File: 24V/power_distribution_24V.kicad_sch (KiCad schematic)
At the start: 23 parts, among them J1 39-30-1040, J2 768250002, J3 39-30-1040, J4 172065-0002, J5 39-30-1040, J6 39-30-1040, J7 2002411213, J8 768250002, U1 RASPBERRY_PCB

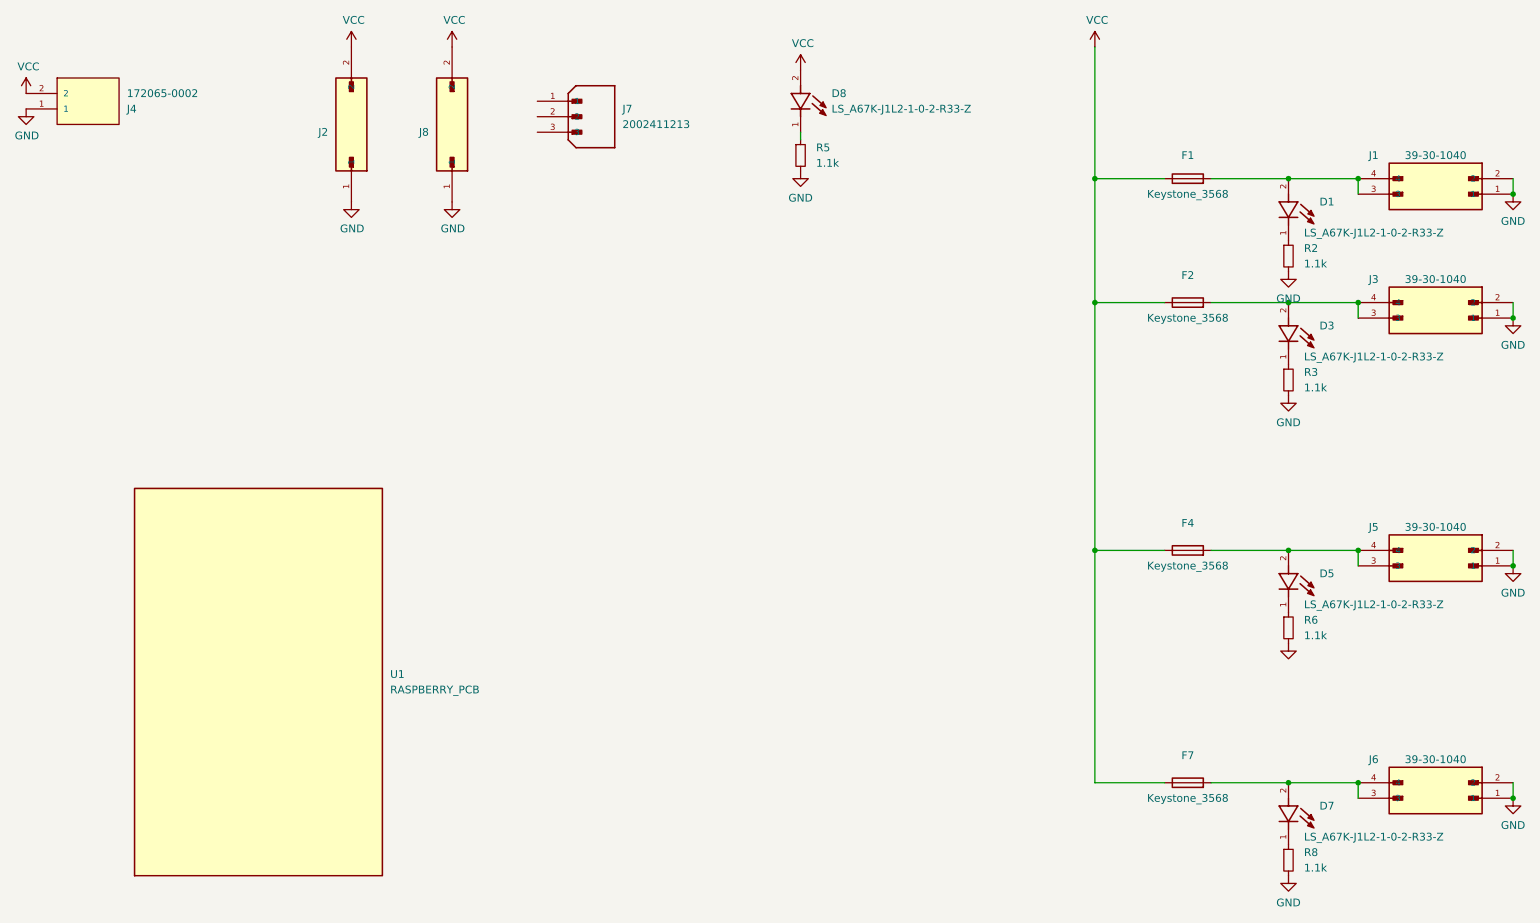
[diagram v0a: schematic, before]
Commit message: corrected resistors for LEDs
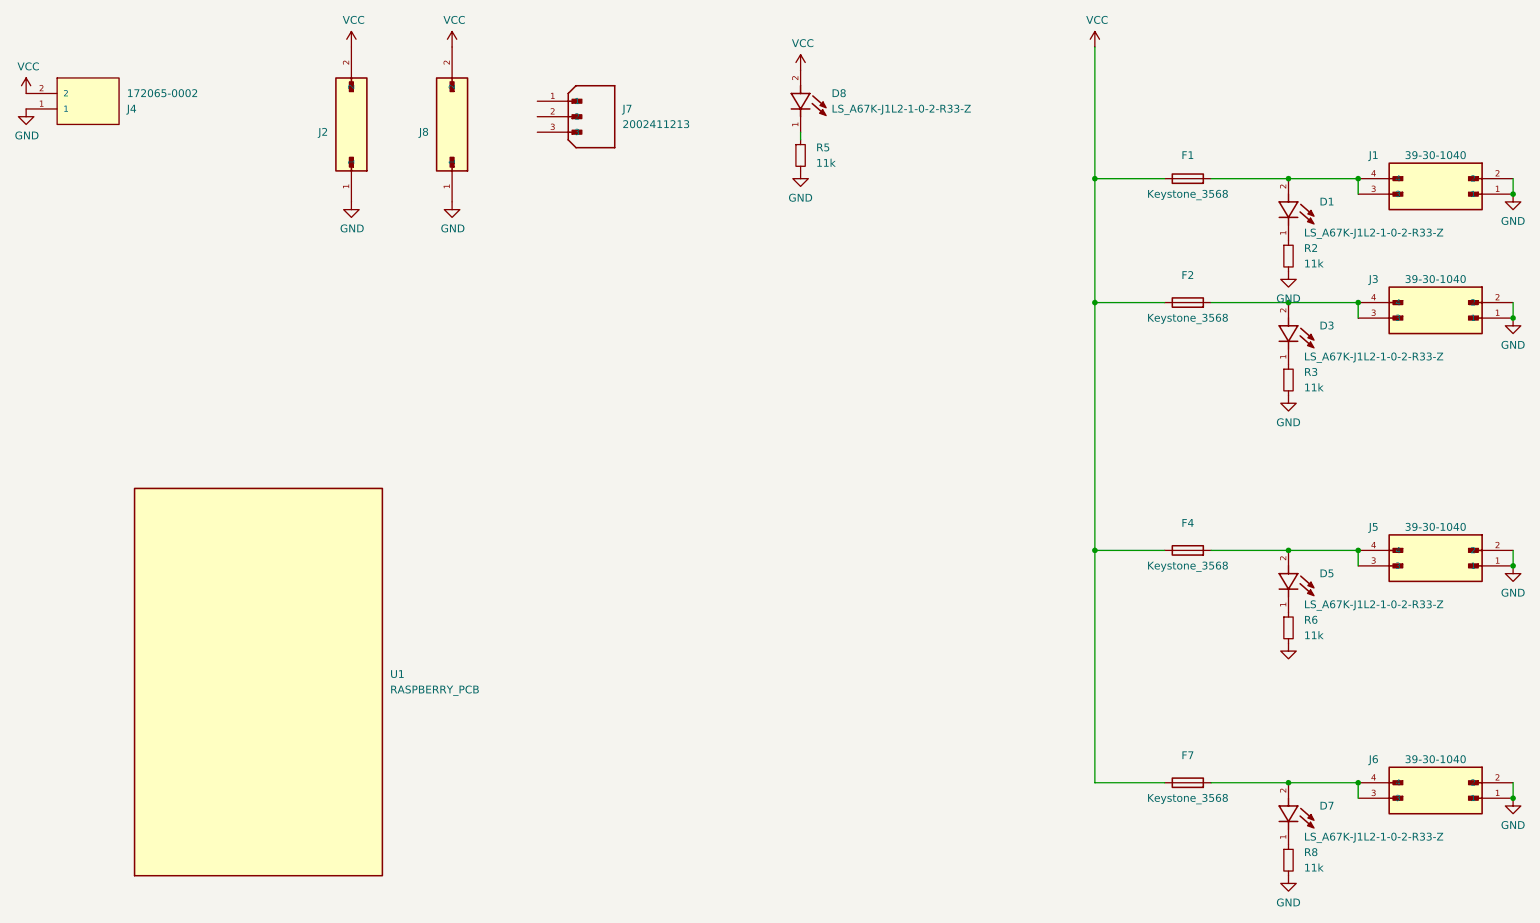
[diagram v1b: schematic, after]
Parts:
- R2, R3, R5, R6, R8: value 1.1k -> 11k
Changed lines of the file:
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@@
       (effects (font (size 1.27 1.27)) (justify left))
     )
-    (property "Value" "1.1k" (at 237.49 54.61 0)
+    (property "Value" "11k" (at 237.49 54.61 0)
       (effects (font (size 1.27 1.27)) (justify left))
     )
@@
       (effects (font (size 1.27 1.27)) (justify left))
     )
-    (property "Value" "1.1k" (at 237.49 153.67 0)
+    (property "Value" "11k" (at 237.49 153.67 0)
       (effects (font (size 1.27 1.27)) (justify left))
     )
@@
       (effects (font (size 1.27 1.27)) (justify left))
     )
-    (property "Value" "1.1k" (at 157.48 38.1 0)
+    (property "Value" "11k" (at 157.48 38.1 0)
       (effects (font (size 1.27 1.27)) (justify left))
     )
@@
       (effects (font (size 1.27 1.27)) (justify left))
     )
-    (property "Value" "1.1k" (at 237.49 74.93 0)
+    (property "Value" "11k" (at 237.49 74.93 0)
       (effects (font (size 1.27 1.27)) (justify left))
     )
@@
       (effects (font (size 1.27 1.27)) (justify left))
     )
-    (property "Value" "1.1k" (at 237.49 115.57 0)
-      (effects (font (size 1.27 1.27)) (justify left))
-    )
+    (property "Value" "11k" (at 237.49 115.57 0)
+      (effects (font (size 1.27 1.27)) (justify left))
+    )

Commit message: added 3d models to the pcbs
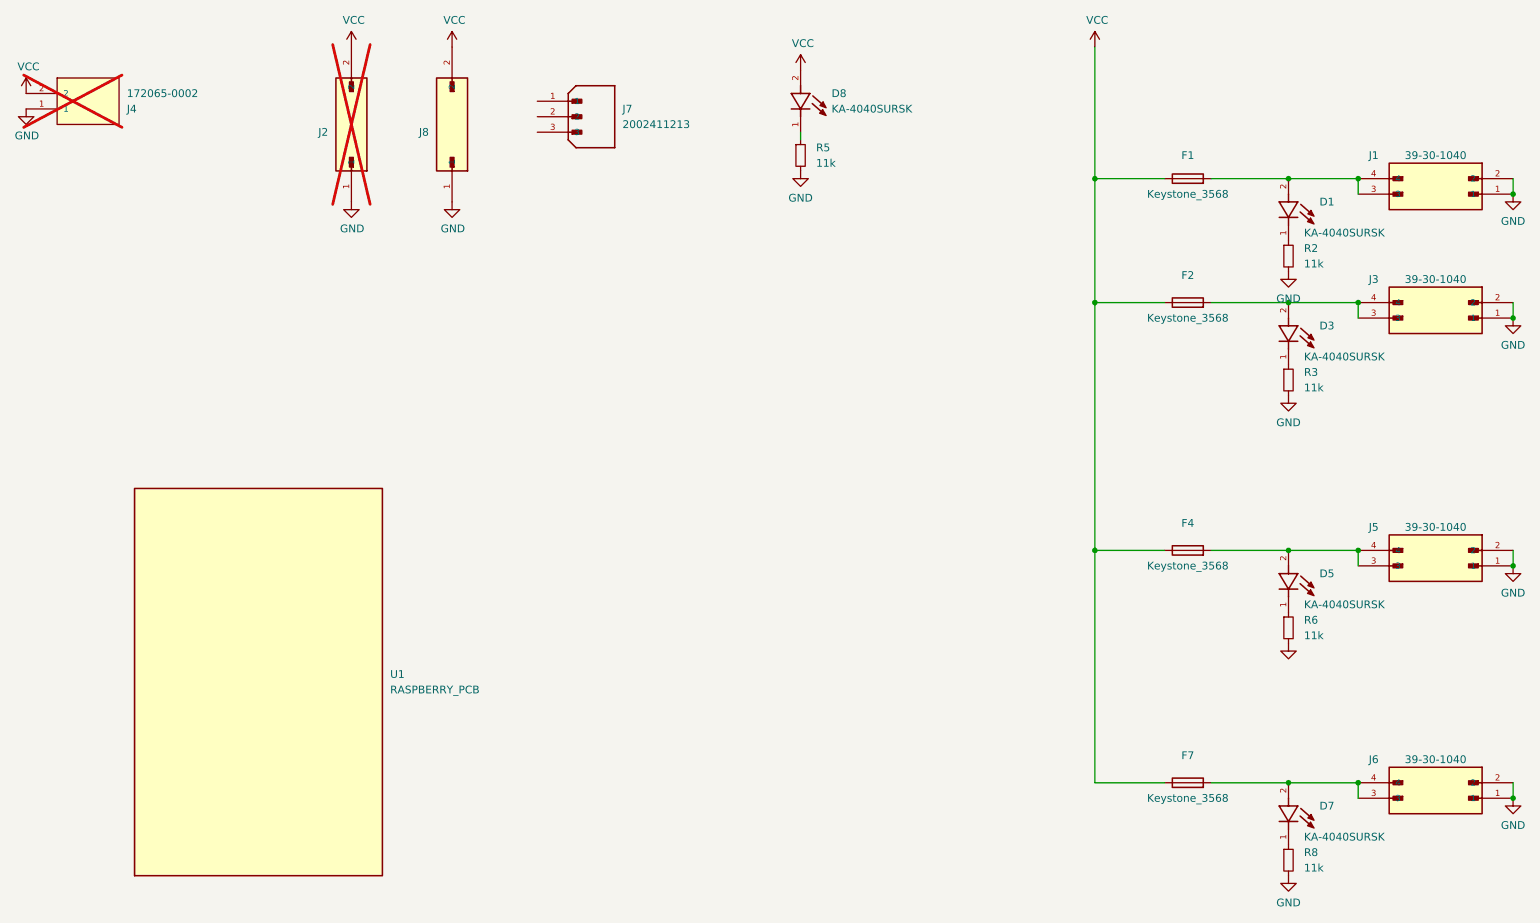
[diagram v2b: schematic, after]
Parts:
- D1, D3, D5, D7, D8: value LS_A67K-J1L2-1-0-2-R33-Z -> KA-4040SURSK
- J2, J4: now not fitted
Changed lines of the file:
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@@
       (effects (font (size 1.27 1.27)) (justify left))
     )
-    (property "Value" "LS_A67K-J1L2-1-0-2-R33-Z" (at 160.02 29.21 90)
+    (property "Value" "KA-4040SURSK" (at 160.02 29.21 90)
       (effects (font (size 1.27 1.27)) (justify left))
     )
@@
       (effects (font (size 1.27 1.27)) (justify left))
     )
-    (property "Value" "LS_A67K-J1L2-1-0-2-R33-Z" (at 237.49 148.59 90)
+    (property "Value" "KA-4040SURSK" (at 237.49 148.59 90)
       (effects (font (size 1.27 1.27)) (justify left))
     )
@@
   )
   (symbol (lib_id "768250002:768250002") (at 81.28 31.75 90) (unit 1)
-    (in_bom yes) (on_board yes) (dnp no)
+    (in_bom yes) (on_board yes) (dnp yes)
     (property "Reference" "J2" (at 77.47 33.02 90)
       (effects (font (size 1.27 1.27)) (justify left))
@@
       (effects (font (size 1.27 1.27)) (justify left))
     )
-    (property "Value" "LS_A67K-J1L2-1-0-2-R33-Z" (at 237.49 69.85 90)
+    (property "Value" "KA-4040SURSK" (at 237.49 69.85 90)
       (effects (font (size 1.27 1.27)) (justify left))
     )
@@
       (effects (font (size 1.27 1.27)) (justify left))
     )
-    (property "Value" "LS_A67K-J1L2-1-0-2-R33-Z" (at 237.49 110.49 90)
+    (property "Value" "KA-4040SURSK" (at 237.49 110.49 90)
       (effects (font (size 1.27 1.27)) (justify left))
     )
@@
   )
   (symbol (lib_id "172065-0002:172065-0002") (at 38.1 26.67 0) (mirror x) (unit 1)
-    (in_bom yes) (on_board yes) (dnp no)
+    (in_bom yes) (on_board yes) (dnp yes)
     (property "Reference" "J4" (at 44.45 29.21 0)
       (effects (font (size 1.27 1.27)) (justify left))
@@
       (effects (font (size 1.27 1.27)) (justify left))
     )
-    (property "Value" "LS_A67K-J1L2-1-0-2-R33-Z" (at 237.49 49.53 90)
-      (effects (font (size 1.27 1.27)) (justify left))
-    )
+    (property "Value" "KA-4040SURSK" (at 237.49 49.53 90)
+      (effects (font (size 1.27 1.27)) (justify left))
+    )
